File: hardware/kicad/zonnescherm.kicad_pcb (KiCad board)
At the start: 2 copper layers, 75 x 75 mm, 33 parts, among them K1 K1-ON/OFF, K2 K1-UP/DOWN, K3 K2-ON/OFF, K4 K2-UP/DOWN, P1 ARDUINO-ISP, P2 CONN_MAINS, P3 CONN_SUNSHADE1, P4 CONN_SUNSHADE2, P5 SWITCHES, U1 IRM-05-5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

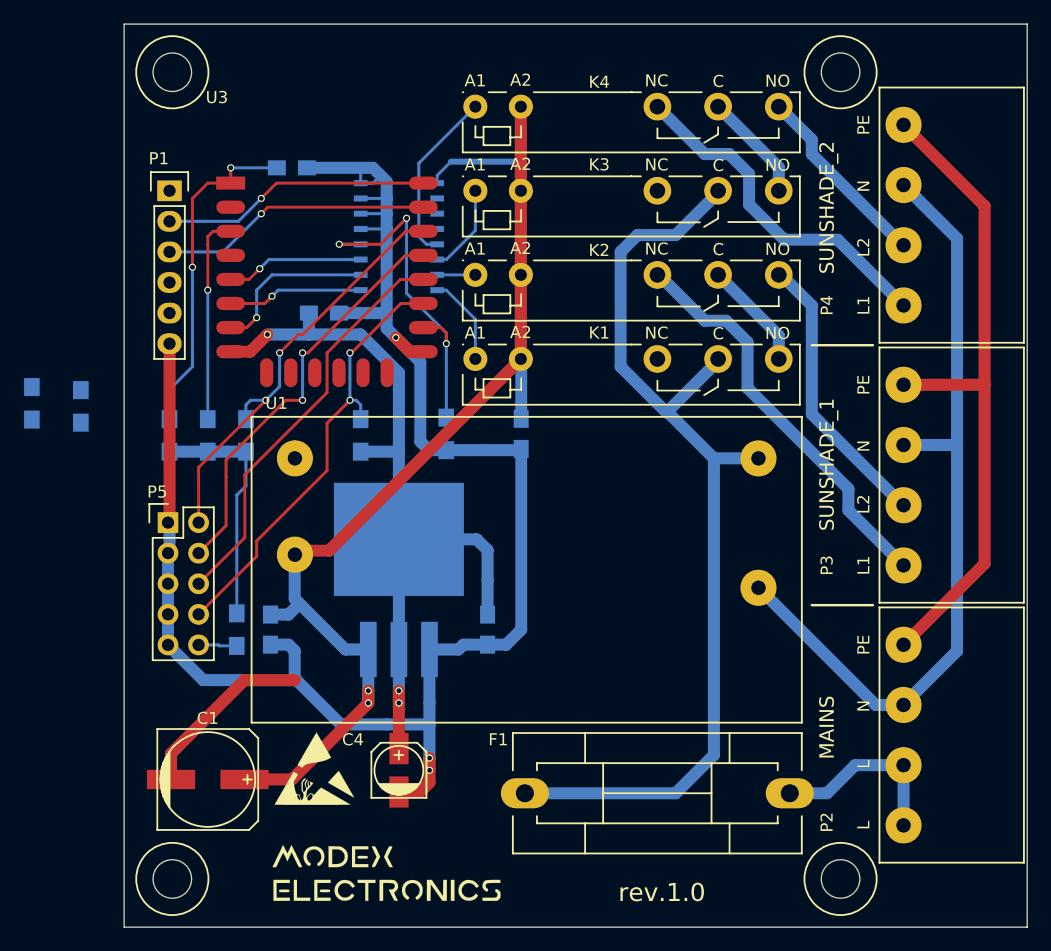
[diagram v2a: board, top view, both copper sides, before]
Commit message: Added picture of the assembled PCB. Changed PCB for release 2.0. Not ready yet.
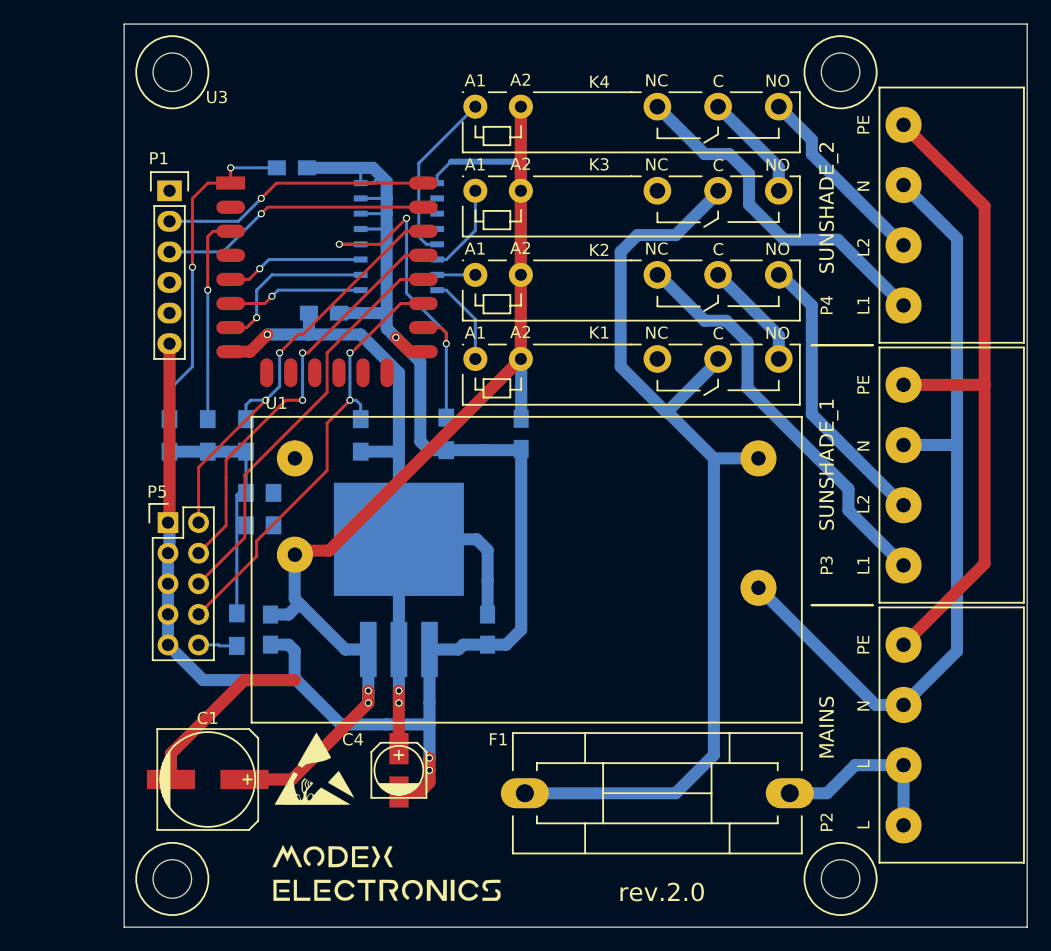
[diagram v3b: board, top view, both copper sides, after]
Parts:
- moved R1 21.9 mm to (120.9, 99.2)
- moved R3 16.2 mm to (118.6, 99.2)
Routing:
- net P3V3: track 95.3 -> 94.2 mm
- net GPIO0: track 34.1 -> 35.2 mm
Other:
- board text added: "rev.2.0"
- board text removed: "rev.1.0"
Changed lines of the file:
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@@
   (general
     (links 80)
-    (no_connects 7)
-    (area 108.05 56.953 183.700501 134.128501)
+    (no_connects 8)
+    (area 97.763 56.953 183.700501 134.128501)
     (thickness 1.6)
     (drawings 18)
@@
   )
   (module Resistors_SMD:R_0805_HandSoldering (layer B.Cu)
-    (at 100.838 90.424 90)
+    (at 120.904 99.2124 90)
     (descr "Resistor SMD 0805, hand soldering")
     (tags "resistor 0805")
@@
   )
   (module Resistors_SMD:R_0805_HandSoldering (layer B.Cu)
-    (at 104.902 90.678 90)
+    (at 118.618 99.2124 90)
     (descr "Resistor SMD 0805, hand soldering")
     (tags "resistor 0805")
@@
     )
   )
-  (gr_text rev.1.0 (at 153.162 131.064) (layer F.SilkS)
+  (gr_text rev.2.0 (at 153.162 131.064) (layer F.SilkS)
     (effects (font (size 1.5 1.5) (thickness 0.2)))
   )
@@
   (segment (start 117.856 107.87) (end 117.856 98.044) (width 0.25) (layer B.Cu) (net 3))
   (segment (start 118.618 97.282) (end 118.618 94.441) (width 0.25) (layer B.Cu) (net 3))
-  (segment (start 117.856 98.044) (end 118.618 97.282) (width 0.25) (layer B.Cu) (net 3))
   (segment (start 131.318 110.871) (end 131.318 114.3) (width 1) (layer B.Cu) (net 3))
   (segment (start 131.318 114.3) (end 131.318 115.316) (width 1) (layer B.Cu) (net 3))
@@
   (segment (start 120.269 90.17) (end 114.681 95.758) (width 0.25) (layer F.Cu) (net 13))
   (via (at 120.269 90.17) (size 0.6) (drill 0.4) (layers F.Cu B.Cu) (net 13))
+  (segment (start 117.856 98.044) (end 118.618 97.282) (width 0.25) (layer B.Cu) (net 14))
   (segment (start 133.348 80.136) (end 131.446 80.136) (width 0.25) (layer F.Cu) (net 14))
   (segment (start 118.5164 101.5746) (end 114.681 105.41) (width 0.25) (layer F.Cu) (net 14))

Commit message: Changed output configuration to enable global usage of the project.
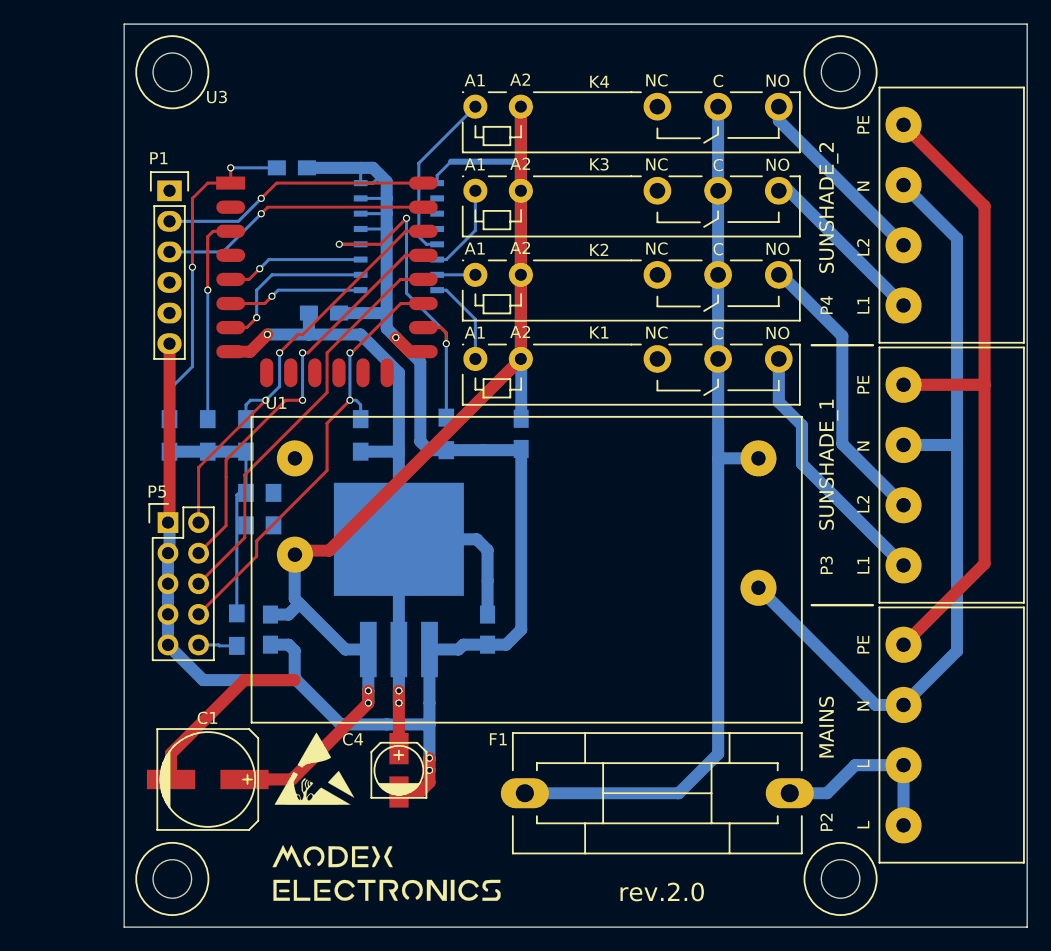
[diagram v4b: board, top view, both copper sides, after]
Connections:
- K2 pad 4: Net-(K1-Pad5) -> P
- K4 pad 4: Net-(K3-Pad5) -> P
- P3 pad 1: Net-(K2-Pad3) -> Net-(K1-Pad5)
- P4 pad 1: Net-(K4-Pad3) -> Net-(K3-Pad5)
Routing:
- net Net-(K2-Pad3): track 34.2 -> 0.63 mm
- net Net-(K4-Pad3): track 28.9 -> 0.13 mm
- net Net-(K1-Pad5): track 9.07 -> 21.4 mm
- net P: track 82.3 -> 74.7 mm
- net Net-(K3-Pad5): track 9.07 -> 14.3 mm
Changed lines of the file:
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@@
     (links 80)
     (no_connects 8)
-    (area 97.763 56.953 183.700501 134.128501)
+    (area 0 0 0 0)
     (thickness 1.6)
     (drawings 18)
-    (tracks 313)
+    (tracks 297)
     (zones 0)
     (modules 33)
@@
   )
   (setup
-    (last_trace_width 0.2)
+    (last_trace_width 1)
     (user_trace_width 0.25)
     (user_trace_width 0.5)
@@
       (net 38 "Net-(K2-Pad5)"))
     (pad 1 thru_hole circle (at 0 0 270) (size 3 3) (drill 1.2) (layers *.Cu *.Mask F.SilkS)
-      (net 39 "Net-(K2-Pad3)"))
+      (net 42 "Net-(K1-Pad5)"))
     (model Relays_ThroughHole.3dshapes/Relay_SPDT_SingleRow_Standing_FinderType34Point51.wrl
       (at (xyz 0 0 0))
@@
       (net 40 "Net-(K4-Pad5)"))
     (pad 1 thru_hole circle (at 0 0 270) (size 3 3) (drill 1.2) (layers *.Cu *.Mask F.SilkS)
-      (net 41 "Net-(K4-Pad3)"))
+      (net 44 "Net-(K3-Pad5)"))
     (model Relays_ThroughHole.3dshapes/Relay_SPDT_SingleRow_Standing_FinderType34Point51.wrl
       (at (xyz 0 0 0))
@@
       (net 38 "Net-(K2-Pad5)"))
     (pad 4 thru_hole circle (at -20.16 0) (size 2.3 2.3) (drill 1.3) (layers *.Cu *.Mask F.SilkS)
-      (net 42 "Net-(K1-Pad5)"))
+      (net 6 P))
     (pad 3 thru_hole circle (at -15.12 0) (size 2.3 2.3) (drill 1.3) (layers *.Cu *.Mask F.SilkS)
       (net 39 "Net-(K2-Pad3)"))
@@
       (net 40 "Net-(K4-Pad5)"))
     (pad 4 thru_hole circle (at -20.16 0) (size 2.3 2.3) (drill 1.3) (layers *.Cu *.Mask F.SilkS)
-      (net 44 "Net-(K3-Pad5)"))
+      (net 6 P))
     (pad 3 thru_hole circle (at -15.12 0) (size 2.3 2.3) (drill 1.3) (layers *.Cu *.Mask F.SilkS)
       (net 41 "Net-(K4-Pad3)"))
@@
   (segment (start 169.211 120.476) (end 173.23 120.476) (width 1) (layer B.Cu) (net 5))
   (segment (start 166.878 122.809) (end 169.211 120.476) (width 1) (layer B.Cu) (net 5))
-  (segment (start 157.48 94.996) (end 157.48 119.634) (width 1) (layer B.Cu) (net 6))
-  (segment (start 154.305 122.809) (end 141.78026 122.809) (width 1) (layer B.Cu) (net 6))
-  (segment (start 157.48 119.634) (end 154.305 122.809) (width 1) (layer B.Cu) (net 6))
-  (segment (start 153.543 91.186) (end 153.67 91.186) (width 1) (layer B.Cu) (net 6))
-  (segment (start 157.48 94.996) (end 161.182 94.996) (width 1) (layer B.Cu) (net 6))
-  (segment (start 153.67 91.186) (end 157.48 94.996) (width 1) (layer B.Cu) (net 6))
-  (segment (start 149.733 87.376) (end 153.543 91.186) (width 1) (layer B.Cu) (net 6))
-  (segment (start 149.733 77.851) (end 149.733 87.376) (width 1) (layer B.Cu) (net 6))
-  (segment (start 151.13 76.454) (end 149.733 77.851) (width 1) (layer B.Cu) (net 6))
-  (segment (start 154.305 76.454) (end 151.13 76.454) (width 1) (layer B.Cu) (net 6))
+  (segment (start 161.182 94.996) (end 157.8864 94.996) (width 1) (layer B.Cu) (net 6) (status 400000))
+  (segment (start 157.8356 95.0468) (end 157.8356 95.0976) (width 1) (layer B.Cu) (net 6))
+  (segment (start 157.8864 94.996) (end 157.8356 95.0468) (width 1) (layer B.Cu) (net 6))
+  (segment (start 157.828 65.786) (end 157.828 72.771) (width 1) (layer B.Cu) (net 6) (status C00000))
+  (segment (start 157.828 72.771) (end 157.828 79.756) (width 1) (layer B.Cu) (net 6) (status C00000))
+  (segment (start 157.828 79.756) (end 157.828 86.741) (width 1) (layer B.Cu) (net 6) (status C00000))
+  (segment (start 157.828 86.741) (end 157.8356 86.7486) (width 1) (layer B.Cu) (net 6) (status C00000))
+  (segment (start 157.8356 86.7486) (end 157.8356 95.0976) (width 1) (layer B.Cu) (net 6) (status 400000))
+  (segment (start 157.8356 95.0976) (end 157.8356 119.5324) (width 1) (layer B.Cu) (net 6))
+  (segment (start 157.8356 119.5324) (end 154.559 122.809) (width 1) (layer B.Cu) (net 6))
+  (segment (start 154.559 122.809) (end 141.78026 122.809) (width 1) (layer B.Cu) (net 6) (status 800000))
   (segment (start 157.828 86.741) (end 157.828 86.901) (width 0.25) (layer B.Cu) (net 6))
-  (segment (start 157.828 86.901) (end 153.543 91.186) (width 1) (layer B.Cu) (net 6))
-  (segment (start 157.828 72.771) (end 157.828 72.931) (width 0.25) (layer B.Cu) (net 6))
-  (segment (start 157.828 72.931) (end 154.305 76.454) (width 1) (layer B.Cu) (net 6))
   (segment (start 133.348 72.136) (end 121.158 72.136) (width 0.25) (layer F.Cu) (net 8))
   (segment (start 117.983 75.311) (end 112.268 75.311) (width 0.25) (layer B.Cu) (net 8))
@@
   (segment (start 177.673 76.739) (end 173.23 72.296) (width 1) (layer B.Cu) (net 37))
   (segment (start 173.355 93.886) (end 173.355 93.98) (width 1) (layer B.Cu) (net 37))
+  (segment (start 162.868 79.756) (end 163.068 79.756) (width 1) (layer B.Cu) (net 38) (status C00000))
+  (segment (start 163.068 79.756) (end 168.148 84.836) (width 1) (layer B.Cu) (net 38) (status 400000))
+  (segment (start 168.148 93.804) (end 173.23 98.886) (width 1) (layer B.Cu) (net 38) (status 800000))
+  (segment (start 168.148 84.836) (end 168.148 93.804) (width 1) (layer B.Cu) (net 38))
   (segment (start 173.23 98.886) (end 173.181 98.886) (width 1) (layer B.Cu) (net 38))
-  (segment (start 173.181 98.886) (end 165.608 91.313) (width 1) (layer B.Cu) (net 38))
-  (segment (start 165.608 82.296) (end 165.608 91.313) (width 1) (layer B.Cu) (net 38))
-  (segment (start 165.608 82.296) (end 163.068 79.756) (width 1) (layer B.Cu) (net 38))
-  (segment (start 162.868 79.756) (end 163.068 79.756) (width 0.25) (layer B.Cu) (net 38))
   (segment (start 152.788 79.756) (end 152.908 79.756) (width 1) (layer B.Cu) (net 39))
-  (segment (start 152.908 79.756) (end 156.718 83.566) (width 1) (layer B.Cu) (net 39))
-  (segment (start 168.656 99.312) (end 173.23 103.886) (width 1) (layer B.Cu) (net 39))
-  (segment (start 168.656 97.536) (end 168.656 99.312) (width 1) (layer B.Cu) (net 39))
-  (segment (start 160.274 89.154) (end 168.656 97.536) (width 1) (layer B.Cu) (net 39))
-  (segment (start 160.274 85.344) (end 160.274 89.154) (width 1) (layer B.Cu) (net 39))
-  (segment (start 158.496 83.566) (end 160.274 85.344) (width 1) (layer B.Cu) (net 39))
-  (segment (start 156.718 83.566) (end 158.496 83.566) (width 1) (layer B.Cu) (net 39))
-  (segment (start 173.23 103.886) (end 173.228 103.886) (width 1) (layer B.Cu) (net 39))
   (segment (start 152.788 79.756) (end 152.788 80.271) (width 0.25) (layer B.Cu) (net 39))
+  (segment (start 162.868 65.786) (end 162.868 66.934) (width 1) (layer B.Cu) (net 40) (status C00000))
+  (segment (start 162.868 66.934) (end 173.23 77.296) (width 1) (layer B.Cu) (net 40) (status C00000))
   (segment (start 173.23 77.296) (end 173.181 77.296) (width 1) (layer B.Cu) (net 40))
-  (segment (start 173.181 77.296) (end 165.608 69.723) (width 1) (layer B.Cu) (net 40))
   (segment (start 173.15 77.216) (end 173.23 77.296) (width 1) (layer B.Cu) (net 40))
-  (segment (start 165.608 68.526) (end 162.868 65.786) (width 1) (layer B.Cu) (net 40))
-  (segment (start 165.608 69.723) (end 165.608 68.526) (width 1) (layer B.Cu) (net 40))
-  (segment (start 173.23 82.296) (end 173.228 82.296) (width 1) (layer B.Cu) (net 41))
-  (segment (start 173.228 82.296) (end 167.767 76.835) (width 1) (layer B.Cu) (net 41))
-  (segment (start 167.767 76.835) (end 163.322 76.835) (width 1) (layer B.Cu) (net 41))
   (segment (start 152.788 65.786) (end 152.788 65.793) (width 1) (layer B.Cu) (net 41))
-  (segment (start 152.788 65.793) (end 156.718 69.723) (width 1) (layer B.Cu) (net 41))
-  (segment (start 160.401 73.914) (end 163.322 76.835) (width 1) (layer B.Cu) (net 41))
-  (segment (start 160.401 71.374) (end 160.401 73.914) (width 1) (layer B.Cu) (net 41))
-  (segment (start 158.75 69.723) (end 160.401 71.374) (width 1) (layer B.Cu) (net 41))
-  (segment (start 156.718 69.723) (end 158.75 69.723) (width 1) (layer B.Cu) (net 41))
   (segment (start 152.788 65.786) (end 152.908 65.786) (width 0.25) (layer B.Cu) (net 41))
-  (segment (start 162.868 86.741) (end 162.868 84.796) (width 1) (layer B.Cu) (net 42))
-  (segment (start 162.868 84.796) (end 157.828 79.756) (width 1) (layer B.Cu) (net 42))
-  (segment (start 162.868 72.771) (end 162.868 70.826) (width 1) (layer B.Cu) (net 44))
-  (segment (start 162.868 70.826) (end 157.828 65.786) (width 1) (layer B.Cu) (net 44))
+  (segment (start 164.7952 92.2528) (end 164.7952 95.4512) (width 1) (layer B.Cu) (net 42))
+  (segment (start 164.7952 95.4512) (end 173.23 103.886) (width 1) (layer B.Cu) (net 42) (status 800000))
+  (segment (start 162.868 86.741) (end 162.868 90.3256) (width 1) (layer B.Cu) (net 42) (status 400000))
+  (segment (start 162.868 90.3256) (end 164.7952 92.2528) (width 1) (layer B.Cu) (net 42))
+  (segment (start 162.868 72.771) (end 163.705 72.771) (width 1) (layer B.Cu) (net 44) (status C00000))
+  (segment (start 163.705 72.771) (end 173.23 82.296) (width 1) (layer B.Cu) (net 44) (status C00000))
+  (segment (start 173.23 82.296) (end 173.228 82.296) (width 1) (layer B.Cu) (net 44))
   (segment (start 117.856 110.57) (end 116.412 110.57) (width 0.25) (layer B.Cu) (net 46))
   (segment (start 116.332 110.49) (end 114.681 110.49) (width 0.25) (layer B.Cu) (net 46))
